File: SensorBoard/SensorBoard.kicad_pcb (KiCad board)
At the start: 2 copper layers, 50 x 50 mm, 9 parts, among them P10 CONN_01X07, P11 CONN_01X07, P15 DHT22, P16 GY-87, P2 CONN_01X04, P3 CONN_01X04

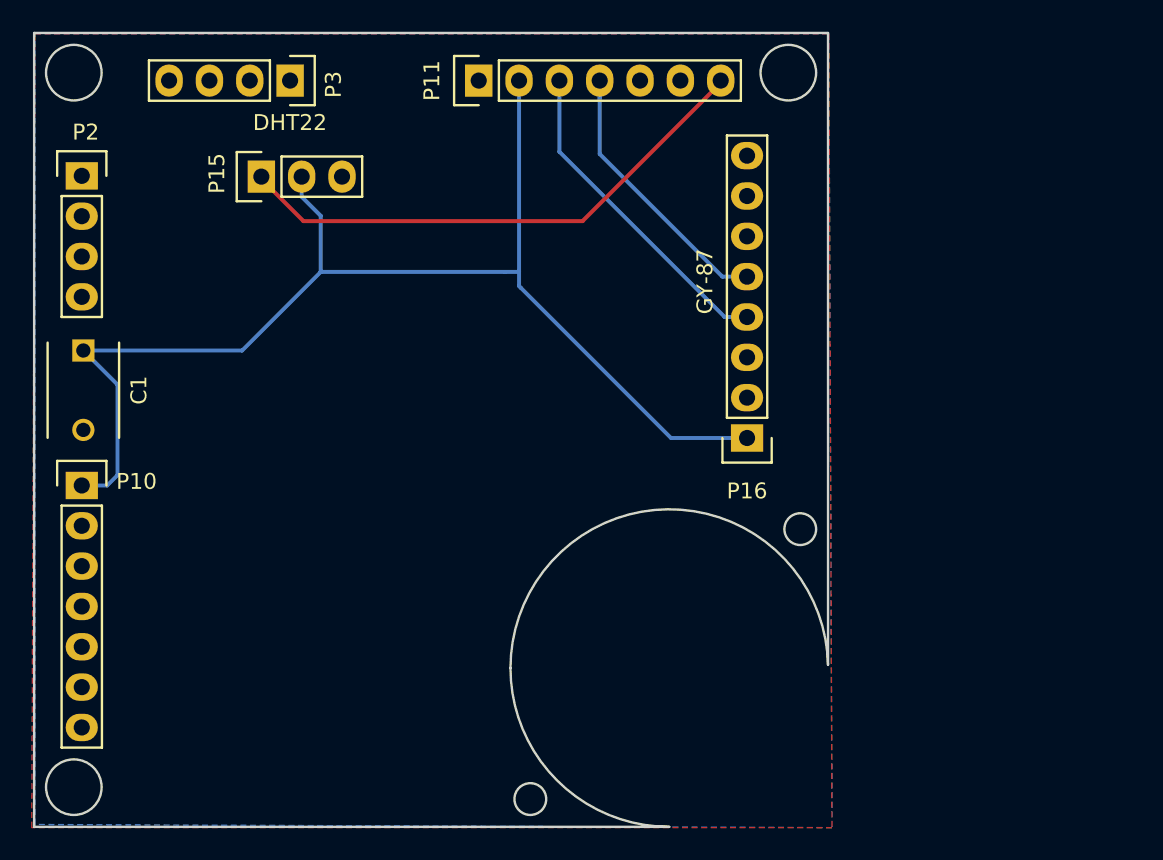
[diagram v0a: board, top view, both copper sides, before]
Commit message: Update PCB referenceschematic SensorBoard
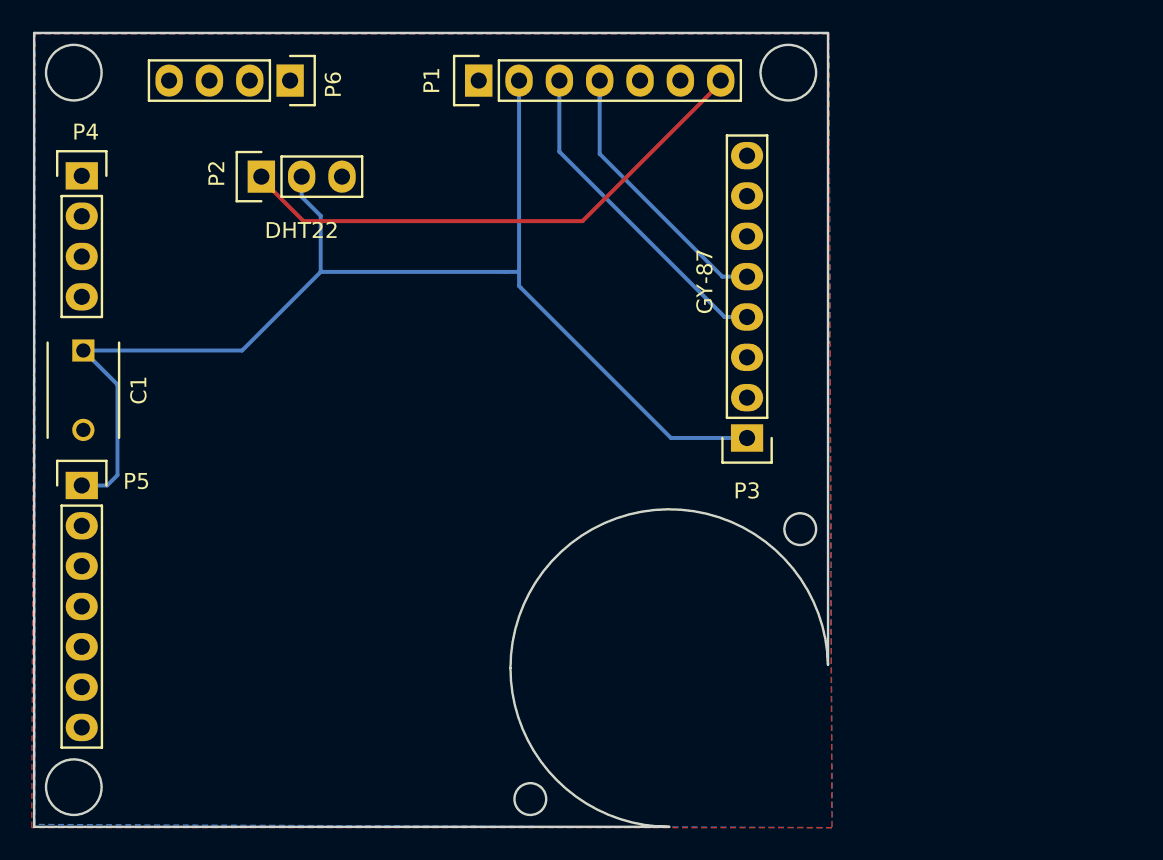
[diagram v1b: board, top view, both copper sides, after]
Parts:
- C1: value C -> 0.1uF
- renumbered P11 to P1, P15 to P2, P16 to P3, P2 to P4, P10 to P5, P3 to P6
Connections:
- net /Sensors/DRDY renamed /DRDY
- net /Sensors/FSYNC renamed /FSYNC
- net /Sensors/INTA renamed /INTA
- net A0 renamed /A0
- net A1 renamed /A1
- net A2 renamed /A2
- net A3 renamed /A3
- net D7 renamed /D7
- net D8 renamed /D8
- net DHT/D6 renamed /DHT/D6
- net INT0 renamed /INT0
- net INT1 renamed /INT1
- net MISO renamed /MISO
- net MOSI renamed /MOSI
- net NSS renamed /NSS
- net RST renamed /RST
- net SCK renamed /SCK
- net SCL renamed /SCL
- net SDA renamed /SDA
- net S_RX renamed /S_RX
- net S_TX renamed /S_TX

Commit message: Update PCB via Sensor Board
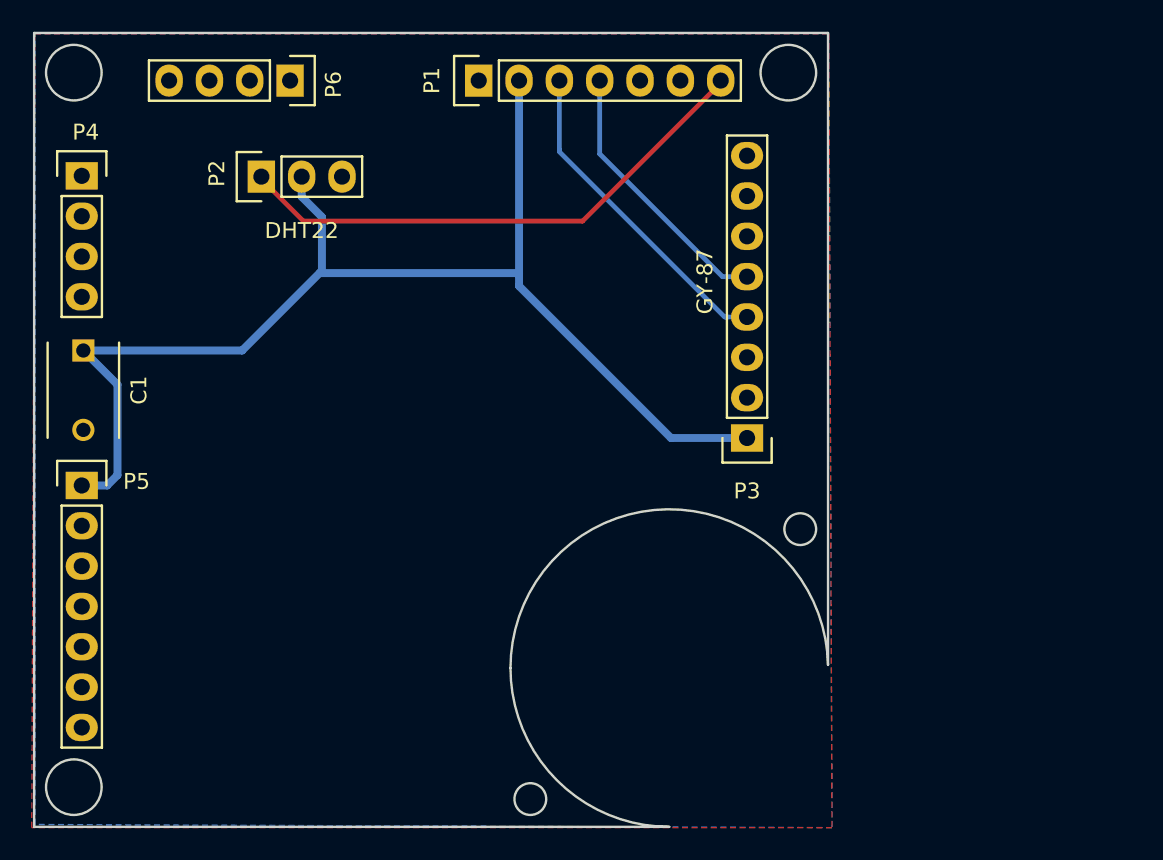
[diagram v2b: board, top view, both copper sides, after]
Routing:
- net +BATT: track 78.5 -> 116.4 mm
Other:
- net class Default: trace_width 0.25 -> 0.3
- net class vcc added: clearance 0.2, trace_width 0.5, via_dia 0.6, via_drill 0.4
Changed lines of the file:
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@@
     (links 11)
     (no_connects 4)
-    (area 72.074999 50.674999 122.225001 100.825001)
+    (area 48.651725 44.05 139.178572 109.450001)
     (thickness 1.6)
     (drawings 23)
-    (tracks 32)
+    (tracks 40)
     (zones 0)
     (modules 9)
@@
   )
   (setup
-    (last_trace_width 0.25)
+    (last_trace_width 0.3)
     (trace_clearance 0.2)
     (zone_clearance 0.8)
@@
   (net_class Default "This is the default net class."
     (clearance 0.2)
-    (trace_width 0.25)
+    (trace_width 0.3)
     (via_dia 0.6)
     (via_drill 0.4)
     (uvia_dia 0.3)
     (uvia_drill 0.1)
-    (add_net +BATT)
     (add_net /A0)
     (add_net /A1)
@@
     (add_net GND)
     (add_net "Net-(P3-Pad2)")
+  )
+  (net_class vcc ""
+    (clearance 0.2)
+    (trace_width 0.5)
+    (via_dia 0.6)
+    (via_drill 0.4)
+    (uvia_dia 0.3)
+    (uvia_drill 0.1)
+    (add_net +BATT)
   )
   (module Pin_Headers:Pin_Header_Straight_1x03 (layer F.Cu)
@@
   (gr_line (start 72.15 100.75) (end 72.15 50.75) (layer Edge.Cuts) (width 0.15))
   (gr_line (start 72.15 50.75) (end 122.15 50.75) (layer Edge.Cuts) (width 0.15))
-  (segment (start 89 59.8) (end 89 61.066) (width 0.25) (layer B.Cu) (net 2))
+  (segment (start 76.75 79.25) (end 75.15 79.25) (width 0.5) (layer B.Cu) (net 2))
+  (segment (start 76.75 79.25) (end 77.4 78.6) (width 0.5) (layer B.Cu) (net 2))
+  (segment (start 75.25 70.75) (end 77.4 72.9) (width 0.5) (layer B.Cu) (net 2))
+  (segment (start 77.4 72.9) (end 77.4 78.6) (width 0.5) (layer B.Cu) (net 2))
+  (segment (start 85.25 70.75) (end 75.25 70.75) (width 0.5) (layer B.Cu) (net 2))
+  (segment (start 90.275 65.875) (end 90.125 65.875) (width 0.5) (layer B.Cu) (net 2))
+  (segment (start 90.125 65.875) (end 85.25 70.75) (width 0.5) (layer B.Cu) (net 2))
+  (segment (start 89 59.8) (end 89 61.066) (width 0.5) (layer B.Cu) (net 2))
+  (segment (start 90.275 65.875) (end 90.275 62.341) (width 0.5) (layer B.Cu) (net 2))
+  (segment (start 90.275 62.341) (end 89 61.066) (width 0.5) (layer B.Cu) (net 2))
+  (segment (start 102.69 65.875) (end 102.69 66.69) (width 0.5) (layer B.Cu) (net 2))
+  (segment (start 102.69 53.75) (end 102.69 65.875) (width 0.5) (layer B.Cu) (net 2))
+  (segment (start 90.275 65.875) (end 90.2 65.8) (width 0.5) (layer B.Cu) (net 2))
+  (segment (start 102.69 65.875) (end 90.275 65.875) (width 0.5) (layer B.Cu) (net 2))
+  (segment (start 117.05 76.26) (end 112.26 76.26) (width 0.5) (layer B.Cu) (net 2))
+  (segment (start 102.69 66.69) (end 112.26 76.26) (width 0.5) (layer B.Cu) (net 2))
   (segment (start 89 61.066) (end 90.2 62.266) (width 0.25) (layer B.Cu) (net 2))
   (segment (start 90.2 62.266) (end 90.2 65.8) (width 0.25) (layer B.Cu) (net 2))
-  (segment (start 75.15 79.25) (end 76.75 79.25) (width 0.25) (layer B.Cu) (net 2))
-  (segment (start 77.4 72.9) (end 75.25 70.75) (width 0.25) (layer B.Cu) (net 2))
-  (segment (start 77.4 78.6) (end 77.4 72.9) (width 0.25) (layer B.Cu) (net 2))
-  (segment (start 76.75 79.25) (end 77.4 78.6) (width 0.25) (layer B.Cu) (net 2))
   (segment (start 101.8 65.8) (end 102.69 65.8) (width 0.25) (layer B.Cu) (net 2))
   (segment (start 102.69 53.75) (end 102.69 65.8) (width 0.25) (layer B.Cu) (net 2))
   (segment (start 102.69 65.8) (end 102.69 66.69) (width 0.25) (layer B.Cu) (net 2))
-  (segment (start 102.69 66.69) (end 102.8 66.8) (width 0.25) (layer B.Cu) (net 2))
   (segment (start 90.2 65.8) (end 101.8 65.8) (width 0.25) (layer B.Cu) (net 2))
-  (segment (start 112.26 76.26) (end 117.05 76.26) (width 0.25) (layer B.Cu) (net 2))
-  (segment (start 102.8 66.8) (end 112.26 76.26) (width 0.25) (layer B.Cu) (net 2))
-  (segment (start 75.25 70.75) (end 85.25 70.75) (width 0.25) (layer B.Cu) (net 2))
   (segment (start 85.25 70.75) (end 90.2 65.8) (width 0.25) (layer B.Cu) (net 2))
-  (segment (start 105.23 58.23) (end 115.64 68.64) (width 0.25) (layer B.Cu) (net 3))
-  (segment (start 115.64 68.64) (end 117.05 68.64) (width 0.25) (layer B.Cu) (net 3))
-  (segment (start 105.23 53.75) (end 105.23 58.23) (width 0.25) (layer B.Cu) (net 3))
+  (segment (start 117.05 68.64) (end 115.64 68.64) (width 0.3) (layer B.Cu) (net 3))
+  (segment (start 115.64 68.64) (end 105.23 58.23) (width 0.3) (layer B.Cu) (net 3))
+  (segment (start 105.23 58.23) (end 105.23 58.1) (width 0.3) (layer B.Cu) (net 3))
+  (segment (start 105.23 58.1) (end 105.23 53.75) (width 0.3) (layer B.Cu) (net 3))
   (segment (start 117.2024 68.64) (end 117.05 68.64) (width 0.25) (layer B.Cu) (net 3))
-  (segment (start 107.77 58.37) (end 115.5 66.1) (width 0.25) (layer B.Cu) (net 4))
-  (segment (start 115.5 66.1) (end 117.05 66.1) (width 0.25) (layer B.Cu) (net 4))
-  (segment (start 107.77 53.75) (end 107.77 58.37) (width 0.25) (layer B.Cu) (net 4))
+  (segment (start 115.5 66.1) (end 117.05 66.1) (width 0.3) (layer B.Cu) (net 4))
+  (segment (start 107.77 58.37) (end 115.5 66.1) (width 0.3) (layer B.Cu) (net 4))
+  (segment (start 107.77 53.75) (end 107.77 58.37) (width 0.3) (layer B.Cu) (net 4))
   (segment (start 117.2024 66.1) (end 117.05 66.1) (width 0.25) (layer B.Cu) (net 4))
   (segment (start 107.77 53.75) (end 107.77 55.016) (width 0.25) (layer B.Cu) (net 4))
-  (segment (start 89.1076 62.6) (end 86.46 59.9524) (width 0.25) (layer F.Cu) (net 7))
-  (segment (start 86.46 59.9524) (end 86.46 59.8) (width 0.25) (layer F.Cu) (net 7))
-  (segment (start 106.6924 62.6) (end 89.1076 62.6) (width 0.25) (layer F.Cu) (net 7))
-  (segment (start 106.6924 62.6) (end 115.39 53.9024) (width 0.25) (layer F.Cu) (net 7))
-  (segment (start 115.39 53.9024) (end 115.39 53.75) (width 0.25) (layer F.Cu) (net 7))
+  (segment (start 86.46 59.8) (end 86.46 59.9524) (width 0.3) (layer F.Cu) (net 7))
+  (segment (start 86.46 59.9524) (end 89.1076 62.6) (width 0.3) (layer F.Cu) (net 7))
+  (segment (start 115.39 53.75) (end 115.39 53.9024) (width 0.3) (layer F.Cu) (net 7))
+  (segment (start 106.6924 62.6) (end 89.1076 62.6) (width 0.3) (layer F.Cu) (net 7))
+  (segment (start 115.39 53.9024) (end 106.6924 62.6) (width 0.3) (layer F.Cu) (net 7))
   (segment (start 115.39 53.5976) (end 115.39 53.75) (width 0.25) (layer F.Cu) (net 7))
   (segment (start 116.8976 73.72) (end 117.05 73.72) (width 0.25) (layer F.Cu) (net 8))
@@
     (connect_pads (clearance 0.8))
     (min_thickness 0.254)
-    (fill (arc_segments 16) (thermal_gap 0.508) (thermal_bridge_width 0.508))
+    (fill yes (arc_segments 16) (thermal_gap 0.508) (thermal_bridge_width 0.508))
     (polygon
       (pts
@@
     (connect_pads (clearance 0.8))
     (min_thickness 0.254)
-    (fill (arc_segments 16) (thermal_gap 0.508) (thermal_bridge_width 0.508))
+    (fill yes (arc_segments 16) (thermal_gap 0.508) (thermal_bridge_width 0.508))
     (polygon
       (pts

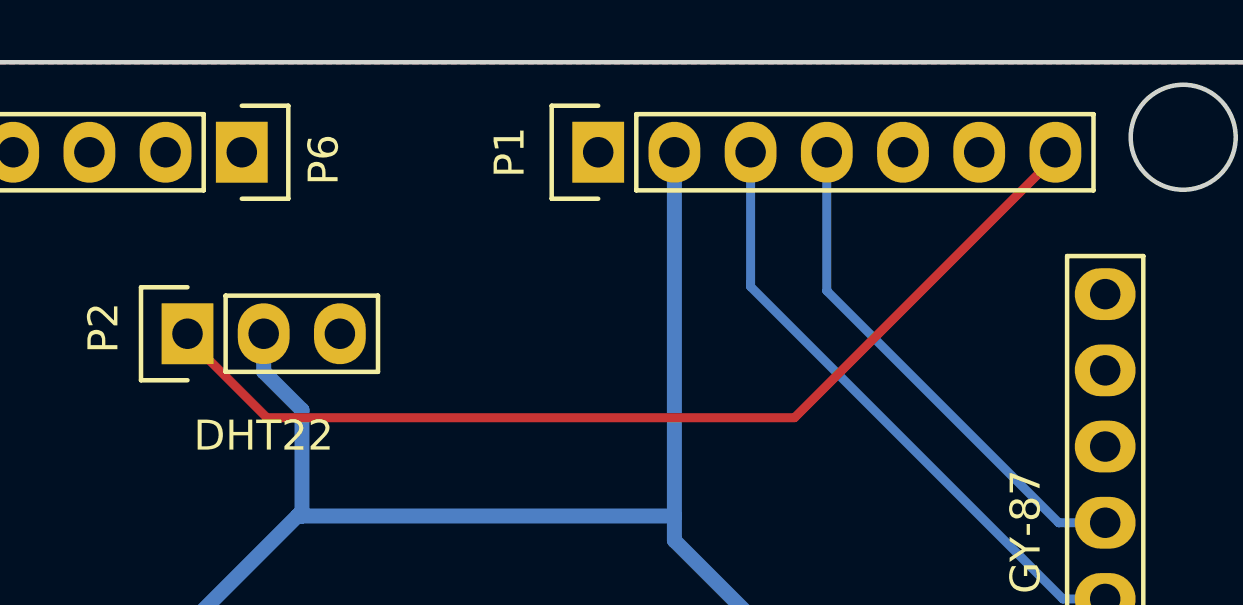
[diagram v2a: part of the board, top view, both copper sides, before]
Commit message: fix via data dht22
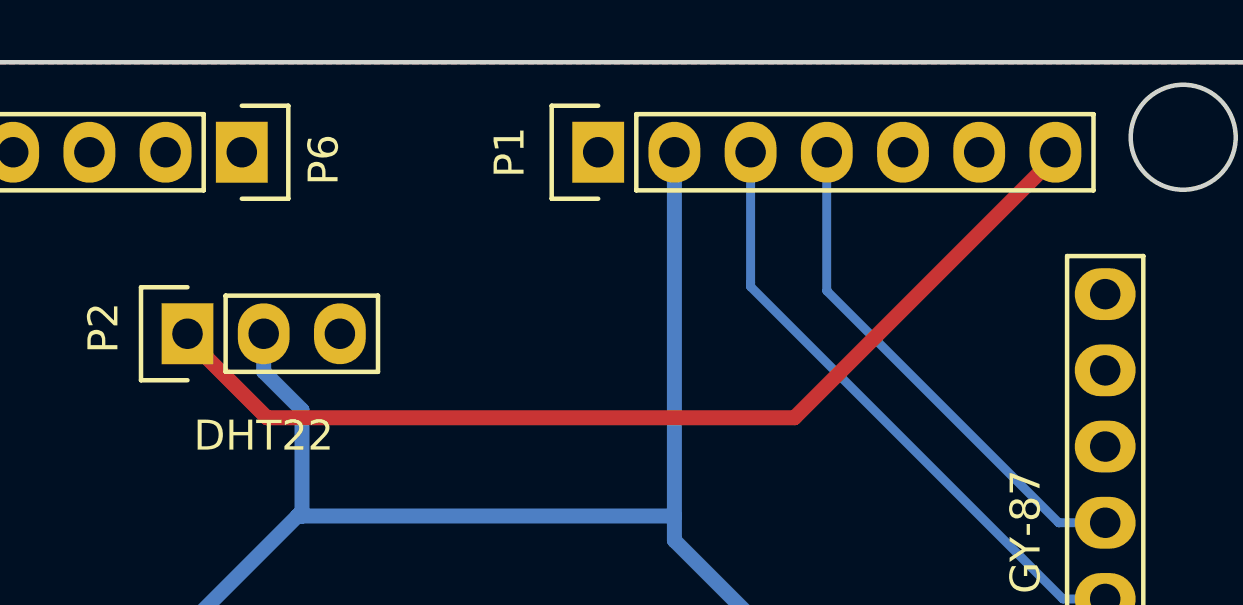
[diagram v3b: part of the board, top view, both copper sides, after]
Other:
- board text added: "Sensor Board CaTSat 1.1v"
- board text removed: "Sensor Board"
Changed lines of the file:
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@@
   (general
     (links 11)
-    (no_connects 4)
-    (area 48.651725 44.05 139.178572 109.450001)
+    (no_connects 0)
+    (area 72.074999 50.674999 122.225001 100.825001)
     (thickness 1.6)
     (drawings 23)
@@
     (fp_line (start -1.99898 -23.50008) (end -1.09982 -21.20138) (layer B.SilkS) (width 0.15))
   )
-  (gr_text "Sensor Board" (at 104.4 64.4) (layer B.SilkS)
+  (gr_text "Sensor Board\nCaTSat 1.1v" (at 104.4 64.4) (layer B.SilkS)
     (effects (font (size 1.5 1.5) (thickness 0.3)) (justify mirror))
   )
@@
   (segment (start 107.77 53.75) (end 107.77 55.016) (width 0.25) (layer B.Cu) (net 4))
   (segment (start 86.46 59.8) (end 86.46 59.9524) (width 0.3) (layer F.Cu) (net 7))
-  (segment (start 86.46 59.9524) (end 89.1076 62.6) (width 0.3) (layer F.Cu) (net 7))
+  (segment (start 86.46 59.9524) (end 89.1076 62.6) (width 0.5) (layer F.Cu) (net 7))
   (segment (start 115.39 53.75) (end 115.39 53.9024) (width 0.3) (layer F.Cu) (net 7))
-  (segment (start 106.6924 62.6) (end 89.1076 62.6) (width 0.3) (layer F.Cu) (net 7))
-  (segment (start 115.39 53.9024) (end 106.6924 62.6) (width 0.3) (layer F.Cu) (net 7))
+  (segment (start 106.6924 62.6) (end 89.1076 62.6) (width 0.5) (layer F.Cu) (net 7))
+  (segment (start 115.39 53.9024) (end 106.6924 62.6) (width 0.5) (layer F.Cu) (net 7))
   (segment (start 115.39 53.5976) (end 115.39 53.75) (width 0.25) (layer F.Cu) (net 7))
   (segment (start 116.8976 73.72) (end 117.05 73.72) (width 0.25) (layer F.Cu) (net 8))
@@
     (connect_pads (clearance 0.8))
     (min_thickness 0.254)
-    (fill yes (arc_segments 16) (thermal_gap 0.508) (thermal_bridge_width 0.508))
+    (fill (arc_segments 16) (thermal_gap 0.508) (thermal_bridge_width 0.508))
     (polygon
       (pts
@@
     (connect_pads (clearance 0.8))
     (min_thickness 0.254)
-    (fill yes (arc_segments 16) (thermal_gap 0.508) (thermal_bridge_width 0.508))
+    (fill (arc_segments 16) (thermal_gap 0.508) (thermal_bridge_width 0.508))
     (polygon
       (pts
